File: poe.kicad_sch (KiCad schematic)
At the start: 59 parts, among them IC1 TPS2378DDA, J1 B2B-XH-A_LF__SN_, J6 SS-74800-144, U3 TPS2373-3RGW, U4 URB4805YMD-30WR3

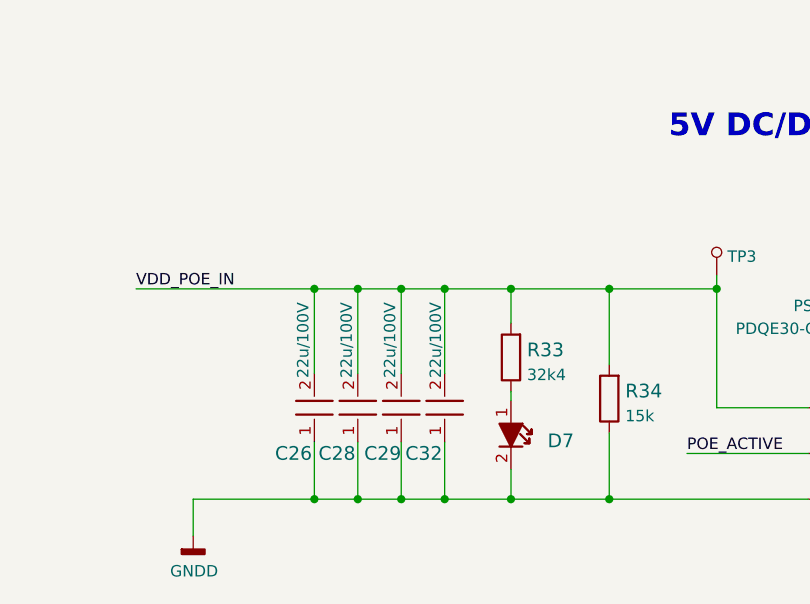
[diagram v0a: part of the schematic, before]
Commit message: Update C26, C28, C29, C32 symbol
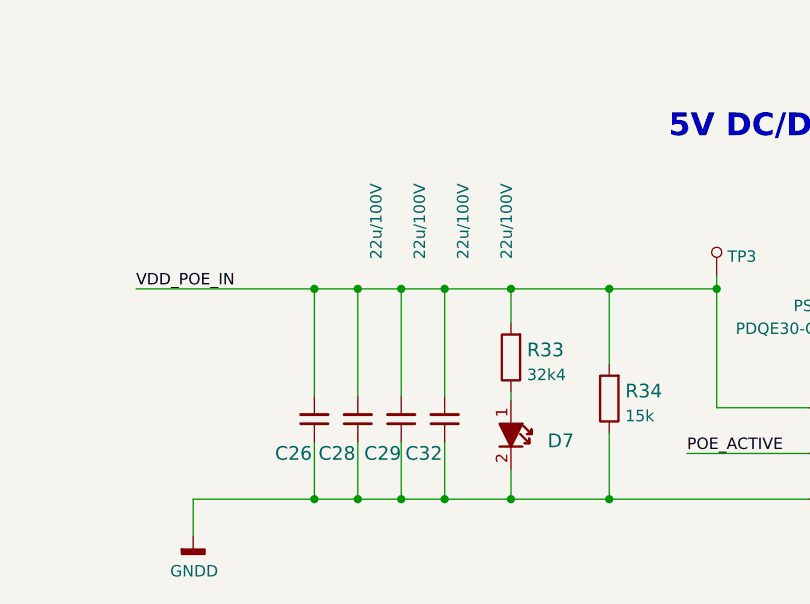
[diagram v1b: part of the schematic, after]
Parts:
- C26, C28, C29, C32: footprint antmicro-footprints:2220-cap -> antmicro-footprints:C_2220_5650Metric; symbol antmicroCapacitorsmisc:C_22u_2220_100V -> antmicroCapacitorsmisc:C_22u_100V_2220

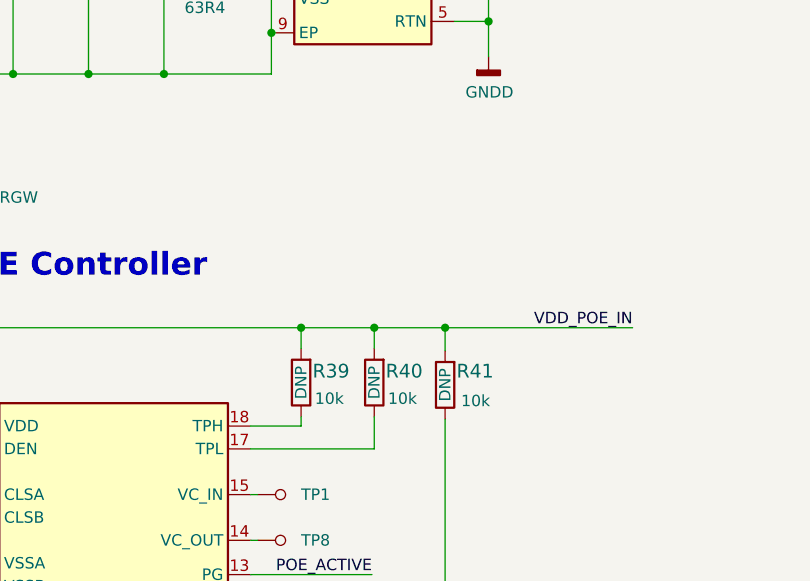
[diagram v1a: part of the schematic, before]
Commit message: Update R5, R9, R10, R11, R12, R13, R14, R19, R55, R65 symbol and footprint
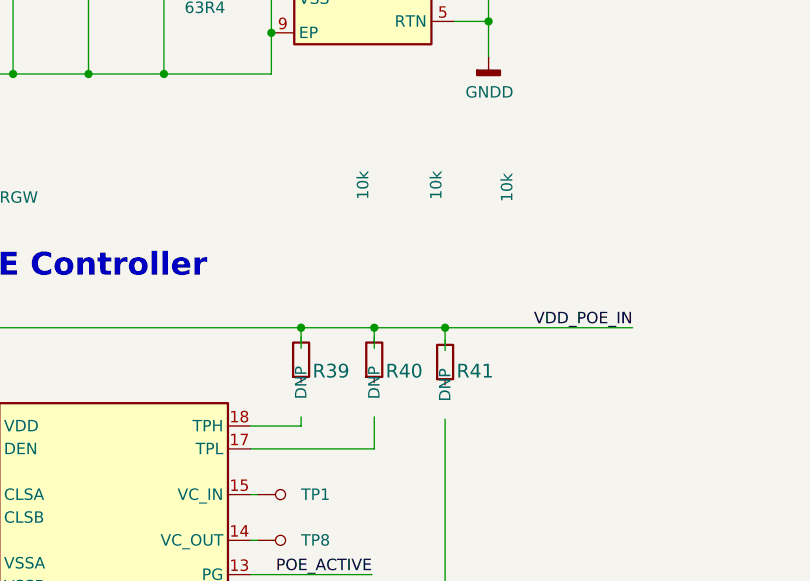
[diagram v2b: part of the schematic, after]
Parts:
- R39, R40, R41: footprint scalenode-cm4-baseboard-footprints:0402-res -> antmicro-footprints:R_0402_1005Metric; symbol scalenode-cm4-baseboard:R_10k_0402 -> antmicroResistors0402:R_10k_0402; Author (none) -> Antmicro; License (none) -> Apache-2.0; MPN CRCW040210K0FKEDHP -> CR0402-FX-1002GLF; Manufacturer VISHAY -> Bourns; Tolerance (none) -> 1%; now in the parts list
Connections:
- net VDD_POE_IN: no longer R39.2, R40.2, R41.2
- net at U3.17 (TPL): no longer R40.1
- net at U3.18 (TPH): no longer R39.1
- net at U3.19 (/BT): no longer R41.1
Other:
- moved on the sheet: R39, R40, R41
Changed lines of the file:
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@@
     (pin "2")
   )
-  (symbol (lib_id "scalenode-cm4-baseboard:R_10k_0402") (at 157.988 214.376 90) (unit 1)
-    (in_bom no) (on_board yes)
+  (symbol (lib_id "antmicroResistors0402:R_10k_0402") (at 157.988 214.376 90) (unit 1)
+    (in_bom yes) (on_board yes)
     (property "Reference" "R41" (id 0) (at 159.258 212.852 90)
       (effects (font (size 1.524 1.524)) (justify right))
@@
       (effects (font (size 1.524 1.524)) hide)
     )
-    (property "Footprint" "scalenode-cm4-baseboard-footprints:0402-res" (id 2) (at 152.908 209.296 0)
-      (effects (font (size 1.524 1.524)) (justify left) hide)
-    )
-    (property "Datasheet" "" (id 3) (at 157.988 214.376 0)
-      (effects (font (size 1.27 1.27)) hide)
-    )
-    (property "Manufacturer" "VISHAY" (id 4) (at 147.828 209.296 0)
-      (effects (font (size 1.524 1.524)) (justify left) hide)
-    )
-    (property "MPN" "CRCW040210K0FKEDHP" (id 5) (at 150.368 209.296 0)
-      (effects (font (size 1.524 1.524)) (justify left) hide)
-    )
-    (property "Val" "10k" (id 6) (at 159.766 216.154 90)
-      (effects (font (size 1.27 1.27)) (justify right))
+    (property "Footprint" "antmicro-footprints:R_0402_1005Metric" (id 2) (at 173.228 194.056 0)
+      (effects (font (size 1.27 1.27) (thickness 0.15)) (justify left bottom) hide)
+    )
+    (property "Datasheet" "https://www.bourns.com/docs/product-datasheets/cr.pdf" (id 3) (at 175.768 194.056 0)
+      (effects (font (size 1.27 1.27) (thickness 0.15)) (justify left bottom) hide)
+    )
+    (property "Manufacturer" "Bourns" (id 4) (at 180.848 194.056 0)
+      (effects (font (size 1.27 1.27) (thickness 0.15)) (justify left bottom) hide)
+    )
+    (property "MPN" "CR0402-FX-1002GLF" (id 5) (at 178.308 194.056 0)
+      (effects (font (size 1.27 1.27) (thickness 0.15)) (justify left bottom) hide)
+    )
+    (property "Val" "10k" (id 6) (at 165.608 194.056 0)
+      (effects (font (size 1.27 1.27) (thickness 0.15)) (justify left bottom))
     )
     (property "DNP" "DNP" (id 7) (at 157.988 214.376 0))
+    (property "License" "Apache-2.0" (id 8) (at 183.388 194.056 0)
+      (effects (font (size 1.27 1.27) (thickness 0.15)) (justify left bottom) hide)
+    )
+    (property "Author" "Antmicro" (id 9) (at 185.928 194.056 0)
+      (effects (font (size 1.27 1.27) (thickness 0.15)) (justify left bottom) hide)
+    )
+    (property "Tolerance" "1%" (id 10) (at 168.148 194.056 0)
+      (effects (font (size 1.27 1.27)) (justify left bottom) hide)
+    )
     (pin "1")
     (pin "2")
@@
     (pin "1")
   )
-  (symbol (lib_id "scalenode-cm4-baseboard:R_10k_0402") (at 141.986 214.122 90) (unit 1)
-    (in_bom no) (on_board yes)
+  (symbol (lib_id "antmicroResistors0402:R_10k_0402") (at 141.986 214.122 90) (unit 1)
+    (in_bom yes) (on_board yes)
     (property "Reference" "R39" (id 0) (at 143.256 212.852 90)
       (effects (font (size 1.524 1.524)) (justify right))
@@
       (effects (font (size 1.524 1.524)) hide)
     )
-    (property "Footprint" "scalenode-cm4-baseboard-footprints:0402-res" (id 2) (at 136.906 209.042 0)
-      (effects (font (size 1.524 1.524)) (justify left) hide)
-    )
-    (property "Datasheet" "" (id 3) (at 141.986 214.122 0)
-      (effects (font (size 1.27 1.27)) hide)
-    )
-    (property "Manufacturer" "VISHAY" (id 4) (at 131.826 209.042 0)
-      (effects (font (size 1.524 1.524)) (justify left) hide)
-    )
-    (property "MPN" "CRCW040210K0FKEDHP" (id 5) (at 134.366 209.042 0)
-      (effects (font (size 1.524 1.524)) (justify left) hide)
-    )
-    (property "Val" "10k" (id 6) (at 143.51 215.9 90)
-      (effects (font (size 1.27 1.27)) (justify right))
+    (property "Footprint" "antmicro-footprints:R_0402_1005Metric" (id 2) (at 157.226 193.802 0)
+      (effects (font (size 1.27 1.27) (thickness 0.15)) (justify left bottom) hide)
+    )
+    (property "Datasheet" "https://www.bourns.com/docs/product-datasheets/cr.pdf" (id 3) (at 159.766 193.802 0)
+      (effects (font (size 1.27 1.27) (thickness 0.15)) (justify left bottom) hide)
+    )
+    (property "Manufacturer" "Bourns" (id 4) (at 164.846 193.802 0)
+      (effects (font (size 1.27 1.27) (thickness 0.15)) (justify left bottom) hide)
+    )
+    (property "MPN" "CR0402-FX-1002GLF" (id 5) (at 162.306 193.802 0)
+      (effects (font (size 1.27 1.27) (thickness 0.15)) (justify left bottom) hide)
+    )
+    (property "Val" "10k" (id 6) (at 149.606 193.802 0)
+      (effects (font (size 1.27 1.27) (thickness 0.15)) (justify left bottom))
     )
     (property "DNP" "DNP" (id 7) (at 141.986 214.122 0))
+    (property "License" "Apache-2.0" (id 8) (at 167.386 193.802 0)
+      (effects (font (size 1.27 1.27) (thickness 0.15)) (justify left bottom) hide)
+    )
+    (property "Author" "Antmicro" (id 9) (at 169.926 193.802 0)
+      (effects (font (size 1.27 1.27) (thickness 0.15)) (justify left bottom) hide)
+    )
+    (property "Tolerance" "1%" (id 10) (at 152.146 193.802 0)
+      (effects (font (size 1.27 1.27)) (justify left bottom) hide)
+    )
     (pin "1")
     (pin "2")
@@
     (pin "2")
   )
-  (symbol (lib_id "scalenode-cm4-baseboard:R_10k_0402") (at 150.114 214.122 90) (unit 1)
-    (in_bom no) (on_board yes)
+  (symbol (lib_id "antmicroResistors0402:R_10k_0402") (at 150.114 214.122 90) (unit 1)
+    (in_bom yes) (on_board yes)
     (property "Reference" "R40" (id 0) (at 151.384 212.852 90)
       (effects (font (size 1.524 1.524)) (justify right))
@@
       (effects (font (size 1.524 1.524)) hide)
     )
-    (property "Footprint" "scalenode-cm4-baseboard-footprints:0402-res" (id 2) (at 145.034 209.042 0)
-      (effects (font (size 1.524 1.524)) (justify left) hide)
-    )
-    (property "Datasheet" "" (id 3) (at 150.114 214.122 0)
-      (effects (font (size 1.27 1.27)) hide)
-    )
-    (property "Manufacturer" "VISHAY" (id 4) (at 139.954 209.042 0)
-      (effects (font (size 1.524 1.524)) (justify left) hide)
-    )
-    (property "MPN" "CRCW040210K0FKEDHP" (id 5) (at 142.494 209.042 0)
-      (effects (font (size 1.524 1.524)) (justify left) hide)
-    )
-    (property "Val" "10k" (id 6) (at 151.638 215.9 90)
-      (effects (font (size 1.27 1.27)) (justify right))
+    (property "Footprint" "antmicro-footprints:R_0402_1005Metric" (id 2) (at 165.354 193.802 0)
+      (effects (font (size 1.27 1.27) (thickness 0.15)) (justify left bottom) hide)
+    )
+    (property "Datasheet" "https://www.bourns.com/docs/product-datasheets/cr.pdf" (id 3) (at 167.894 193.802 0)
+      (effects (font (size 1.27 1.27) (thickness 0.15)) (justify left bottom) hide)
+    )
+    (property "Manufacturer" "Bourns" (id 4) (at 172.974 193.802 0)
+      (effects (font (size 1.27 1.27) (thickness 0.15)) (justify left bottom) hide)
+    )
+    (property "MPN" "CR0402-FX-1002GLF" (id 5) (at 170.434 193.802 0)
+      (effects (font (size 1.27 1.27) (thickness 0.15)) (justify left bottom) hide)
+    )
+    (property "Val" "10k" (id 6) (at 157.734 193.802 0)
+      (effects (font (size 1.27 1.27) (thickness 0.15)) (justify left bottom))
     )
     (property "DNP" "DNP" (id 7) (at 150.114 214.122 0))
-    (pin "1")
-    (pin "2")
+    (property "License" "Apache-2.0" (id 8) (at 175.514 193.802 0)
+      (effects (font (size 1.27 1.27) (thickness 0.15)) (justify left bottom) hide)
+    )
+    (property "Author" "Antmicro" (id 9) (at 178.054 193.802 0)
+      (effects (font (size 1.27 1.27) (thickness 0.15)) (justify left bottom) hide)
+    )
+    (property "Tolerance" "1%" (id 10) (at 160.274 193.802 0)
+      (effects (font (size 1.27 1.27)) (justify left bottom) hide)
+    )
+    (pin "1")
+    (pin "2")

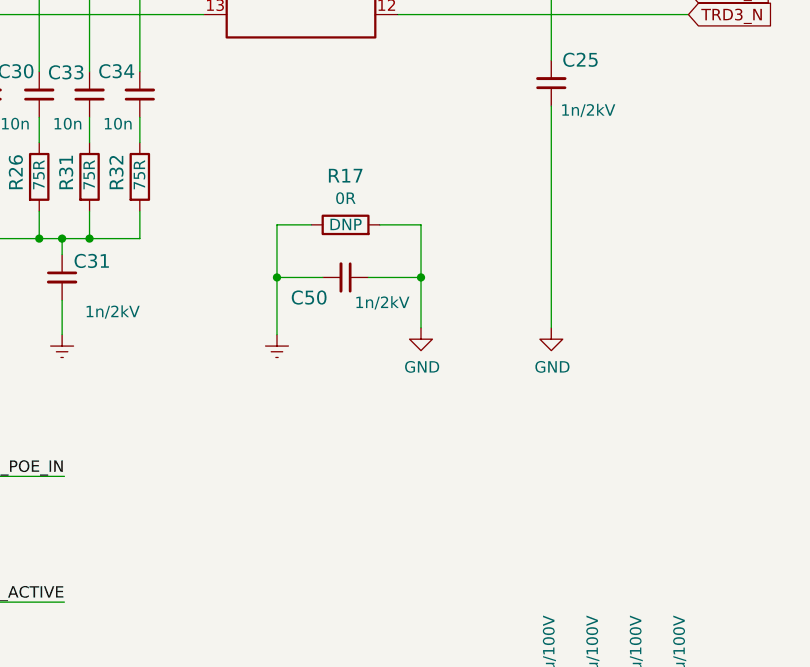
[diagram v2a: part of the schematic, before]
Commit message: Update R17, R62, R63 symbol and footprint
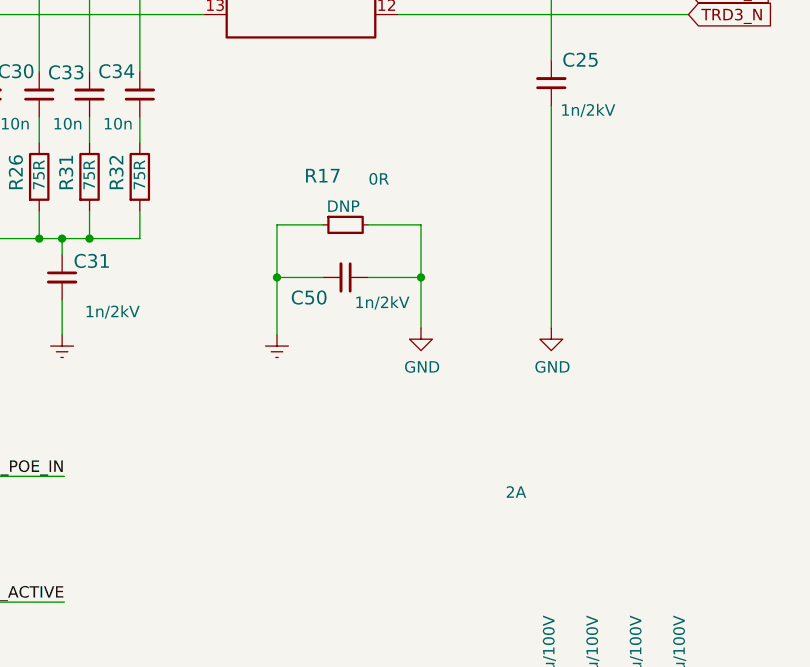
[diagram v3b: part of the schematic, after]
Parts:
- R17: footprint scalenode-cm4-baseboard-footprints:1206-res -> antmicro-footprints:R_1206_3216Metric; symbol scalenode-cm4-baseboard:R_0R_1206 -> antmicroResistorsmisc:R_0R_1206; Author (none) -> Antmicro; Current (none) -> 2A; License (none) -> Apache-2.0; Manufacturer MULTICOMP -> Multicomp
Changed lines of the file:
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@@
     (stroke (width 0) (type default) (color 0 0 0 0))
   )
-  (wire (pts (xy 209.804 121.92) (xy 214.376 121.92))
+  (wire (pts (xy 208.534 121.92) (xy 214.376 121.92))
     (stroke (width 0) (type default) (color 0 0 0 0))
   )
@@
     (stroke (width 0) (type default) (color 0 0 0 0))
   )
-  (wire (pts (xy 198.374 121.92) (xy 202.184 121.92))
+  (wire (pts (xy 198.374 121.92) (xy 203.454 121.92))
     (stroke (width 0) (type default) (color 0 0 0 0))
   )
@@
     (pin "1")
   )
-  (symbol (lib_id "scalenode-cm4-baseboard:R_0R_1206") (at 205.994 121.92 0) (unit 1)
+  (symbol (lib_id "antmicroResistorsmisc:R_0R_1206") (at 203.454 121.92 0) (unit 1)
     (in_bom yes) (on_board yes)
-    (property "Reference" "R17" (id 0) (at 205.994 116.5098 0)
+    (property "Reference" "R17" (id 0) (at 203.454 116.5098 0)
       (effects (font (size 1.524 1.524)))
     )
-    (property "Value" "R_0R_1206" (id 1) (at 205.994 125.73 0)
+    (property "Value" "R_0R_1206" (id 1) (at 203.454 125.73 0)
       (effects (font (size 1.524 1.524)) hide)
     )
-    (property "Footprint" "scalenode-cm4-baseboard-footprints:1206-res" (id 2) (at 211.074 116.84 0)
-      (effects (font (size 1.524 1.524)) (justify left) hide)
-    )
-    (property "Datasheet" "" (id 3) (at 205.994 121.92 0)
-      (effects (font (size 1.27 1.27)) hide)
-    )
-    (property "Manufacturer" "MULTICOMP" (id 4) (at 211.074 111.76 0)
-      (effects (font (size 1.524 1.524)) (justify left) hide)
-    )
-    (property "MPN" "MCMR12X000_PTL" (id 5) (at 211.074 114.3 0)
-      (effects (font (size 1.524 1.524)) (justify left) hide)
-    )
-    (property "Val" "0R" (id 6) (at 205.994 118.999 0))
-    (property "DNP" "DNP" (id 7) (at 205.994 121.92 0))
+    (property "Footprint" "antmicro-footprints:R_1206_3216Metric" (id 2) (at 223.774 137.16 0)
+      (effects (font (size 1.27 1.27) (thickness 0.15)) (justify left bottom) hide)
+    )
+    (property "Datasheet" "https://www.farnell.com/datasheets/2860635.pdf" (id 3) (at 223.774 139.7 0)
+      (effects (font (size 1.27 1.27) (thickness 0.15)) (justify left bottom) hide)
+    )
+    (property "Manufacturer" "Multicomp" (id 4) (at 223.774 144.78 0)
+      (effects (font (size 1.27 1.27) (thickness 0.15)) (justify left bottom) hide)
+    )
+    (property "MPN" "MCMR12X000_PTL" (id 5) (at 223.774 142.24 0)
+      (effects (font (size 1.27 1.27) (thickness 0.15)) (justify left bottom) hide)
+    )
+    (property "Val" "0R" (id 6) (at 208.534 117.602 0)
+      (effects (font (size 1.27 1.27) (thickness 0.15)) (justify left bottom))
+    )
+    (property "DNP" "DNP" (id 7) (at 205.74 119.888 0))
+    (property "License" "Apache-2.0" (id 8) (at 223.774 147.32 0)
+      (effects (font (size 1.27 1.27) (thickness 0.15)) (justify left bottom) hide)
+    )
+    (property "Author" "Antmicro" (id 9) (at 223.774 149.86 0)
+      (effects (font (size 1.27 1.27) (thickness 0.15)) (justify left bottom) hide)
+    )
+    (property "Tolerance" "~" (id 10) (at 223.774 132.08 0)
+      (effects (font (size 1.27 1.27)) (justify left bottom) hide)
+    )
+    (property "Current" "2A" (id 11) (at 223.774 152.4 0)
+      (effects (font (size 1.27 1.27) (thickness 0.15)) (justify left bottom))
+    )
     (pin "1")
     (pin "2")
